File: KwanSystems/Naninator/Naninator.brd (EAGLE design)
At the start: 43.2 x 17.8 mm, 28 parts, among them J001 USB_MICROB_JSTGCT, J002 M15, J003 M15, U001 FT232RLSSOP, U401 ATMEGA328P, Y401 16MHz

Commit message: Pinewood got a mind transplant from Rocketometer
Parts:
- removed D022: BLUE, SparkFun-LED:LED-0603
- removed D023: RED, SparkFun-LED:LED-0603
- removed D401: GREEN, SparkFun-LED:LED-0603
- removed JP1, JP2: (no value), SparkFun-Connectors:1X03
- added U$3: SMLP36RGB2W(R), KwanSystems:SMLP36
- R001: value 680 -> 1.5k
- Y401: device KwanSystems:CRYSTAL_SMD_2MM_2_5MM -> KwanSystems:CRYSTAL_SMD_2MM_1_6MM
- moved C201 17.3 mm to (21.3, 4.57), turned to 180 degrees
- moved D001 15.9 mm to (21.3, 11.9), turned to 90 degrees
- moved C203 14.7 mm to (21.3, 9.14), turned to 180 degrees
- moved U201 14.7 mm to (21.3, 6.86), turned to 90 degrees
- moved C418 4.54 mm to (17.8, 4.32), turned to 0 degrees
- moved C404 2.90 mm to (6.60, 10.2)
- moved C406 2.90 mm to (6.60, 8.89)
- moved C407 2.90 mm to (6.60, 7.62)
- moved Y401 2.90 mm to (6.60, 5.84)
- moved C420 2.79 mm to (19.1, 9.40)
- moved R429 2.79 mm to (8.64, 13.2)
- moved U401 2.79 mm to (13.2, 8.89)
- moved C002 1.37 mm to (25.1, 4.06)
- moved R001 0.57 mm to (25.1, 9.91)
- moved C408 0.36 mm to (6.60, 4.06), turned to 180 degrees
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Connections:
- net N$1 renamed XTAL1
- net N$2 renamed XTAL2
- removed net D11: J002.14, JP2.2, U401.15
- removed net D12: J002.15, JP1.1, U401.16
- removed net D13: J003.1, JP1.2, R001.5, U401.17
- removed net N$11: D022.A, R001.2
- removed net N$9: D023.A, R001.1
- new net D11/MOSI: J002.14, U401.15
- new net D12/MISO: J002.15, U401.16
- new net D13/SCK: J003.1, R001.5, U401.17
- new net N$6: R001.3, U$3.2
- new net N$7: R001.2, U$3.4
- net GND: now also U$3.5; no longer D401.C, JP2.1
- net N$5: now also R001.1, U$3.6; no longer D401.A, R001.3
- net RESET: no longer JP1.3
- net RXLED1: now also U$3.1; no longer R001.7
- net TXLED1: now also U$3.3; no longer R001.8
- net VCC: now also R001.7, R001.8; no longer D022.C, D023.C, JP2.3
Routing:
- net GND: track 0.00 -> 102.1 mm
- net D12: track 62.1 -> 0.00 mm, vias 7 -> 0
- net D13: track 51.9 -> 0.00 mm, vias 4 -> 0
- net D11: track 47.9 -> 0.00 mm, vias 4 -> 0
- net D13/SCK: track 0.00 -> 39.3 mm, vias 0 -> 4
- net RESET: track 74.5 -> 49.8 mm, vias 6 -> 3
- net AREF: track 18.0 -> 40.4 mm, vias 1 -> 3
- net D9: track 18.1 -> 38.8 mm, vias 2 -> 7
- net VBUS: track 38.7 -> 21.0 mm
- net VIN: track 11.7 -> 26.4 mm, vias 2 -> 3
- net D2: track 13.7 -> 26.7 mm, vias 2 -> 5
- net D1: track 43.7 -> 53.5 mm, vias 4 -> 7
- net D7: track 13.5 -> 21.4 mm, vias 0 -> 1
- net D10: track 19.8 -> 26.2 mm, vias 0 -> 3
- net D6: track 11.8 -> 17.6 mm, vias 0 -> 1
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- removed copper zone on layer 1, net GND
- removed copper zone on layer 16, net GND

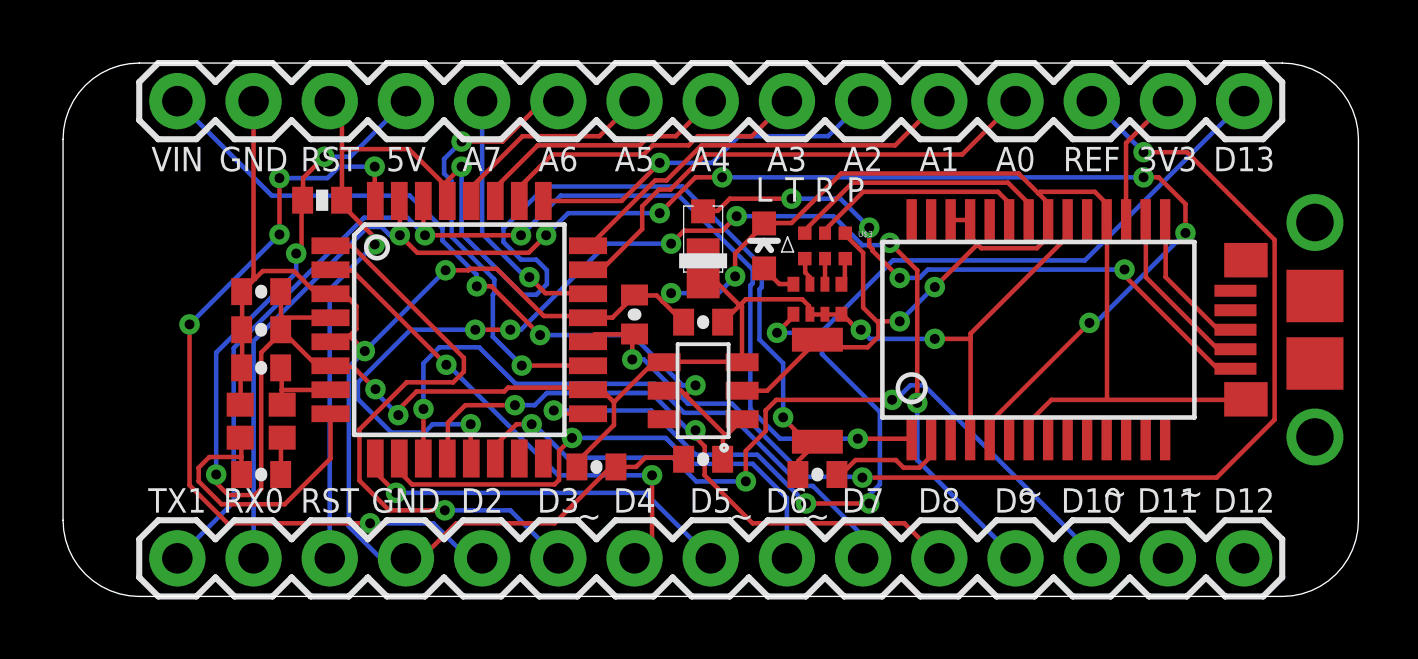
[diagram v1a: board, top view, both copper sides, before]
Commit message: Added Pinewood bench data and K2
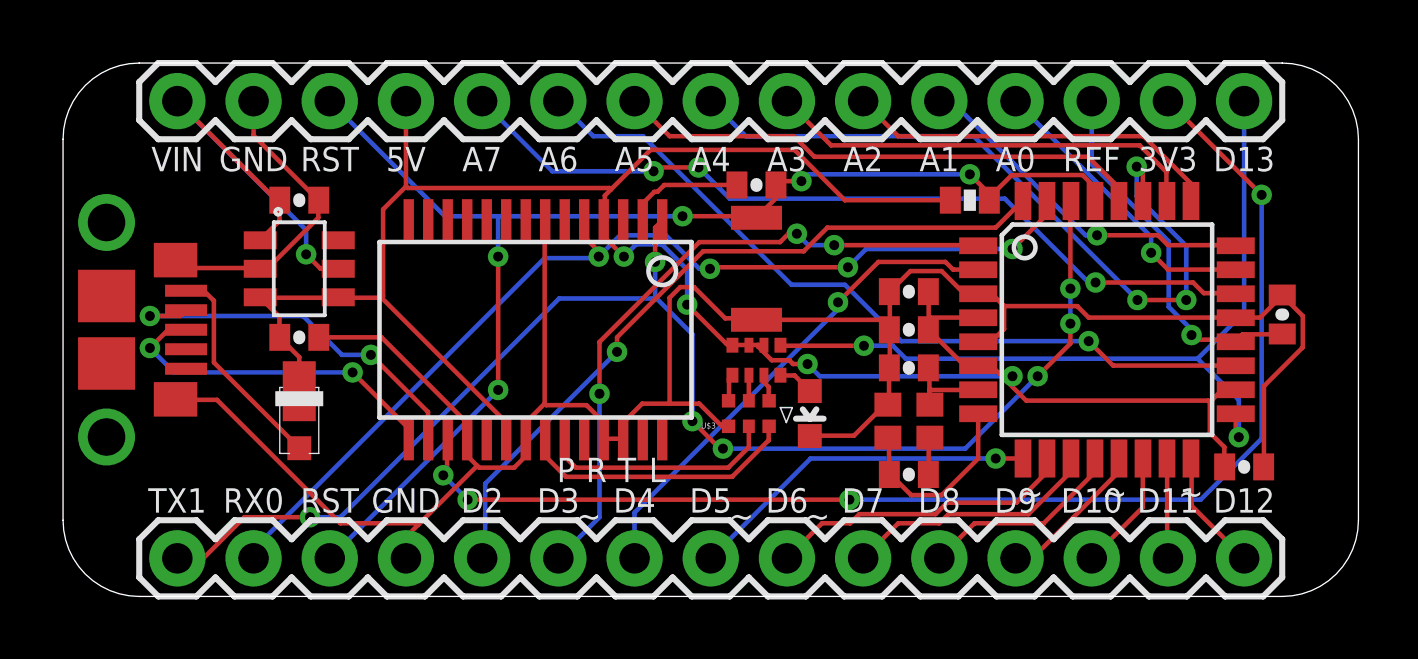
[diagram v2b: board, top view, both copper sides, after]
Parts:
- moved J001 43.2 mm to (0.00, 8.89), turned to 270 degrees
- moved U401 21.6 mm to (34.8, 8.89)
- moved C404 21.6 mm to (28.2, 10.2)
- moved C406 21.6 mm to (28.2, 8.89)
- moved C407 21.6 mm to (28.2, 7.62)
- moved C408 21.6 mm to (28.2, 4.06)
- moved C420 21.6 mm to (40.6, 9.40)
- moved R429 21.6 mm to (30.2, 13.2)
- moved Y401 21.6 mm to (28.2, 5.84)
- moved C418 21.6 mm to (39.4, 4.32)
- moved U001 16.8 mm to (15.7, 8.89), turned to 180 degrees
- moved C201 16.0 mm to (7.87, 13.2), turned to 0 degrees
- moved D001 14.8 mm to (7.87, 5.84), turned to 270 degrees
- moved U201 14.1 mm to (7.87, 10.9), turned to 270 degrees
- moved C203 13.5 mm to (7.87, 8.64), turned to 0 degrees
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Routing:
- net 3V3: track 4.55 -> 42.3 mm, vias 0 -> 4
- net D9: track 38.8 -> 5.09 mm, vias 7 -> 0
- net AREF: track 40.4 -> 12.4 mm, vias 3 -> 1
- net D10: track 26.2 -> 4.04 mm, vias 3 -> 0
- net D1: track 53.5 -> 34.2 mm, vias 7 -> 4
- net A7: track 8.79 -> 27.9 mm, vias 1 -> 3
- net A4: track 8.83 -> 25.0 mm, vias 0 -> 3
- net D8: track 21.0 -> 6.83 mm, vias 2 -> 0
- net VBUS: track 21.0 -> 7.16 mm, vias 4 -> 0
- net D7: track 21.4 -> 8.57 mm, vias 1 -> 0
- net D13/SCK: track 39.3 -> 27.3 mm, vias 4 -> 2
- net VIN: track 26.4 -> 14.5 mm, vias 3 -> 1
- net A6: track 14.8 -> 26.2 mm, vias 2 -> 1
- net A5: track 7.09 -> 17.8 mm
- net GND: track 102.1 -> 92.6 mm, vias 6 -> 0
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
